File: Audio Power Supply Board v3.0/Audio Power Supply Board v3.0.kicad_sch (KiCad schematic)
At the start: 8 parts, among them J1 Conn_01x03_Female

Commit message: Change to a modular drawing and design
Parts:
- added C5, C6, C7, C8: 680µF/200V, Capacitor_THT:CP_Radial_D25.0mm_P10.00mm_SnapIn, symbol Device:C_Polarized_Small
- added D10, D11: 1N4001, Diode_THT:D_DO-41_SOD81_P10.16mm_Horizontal, symbol Diode:1N4001
- added D4, D5: D_x2_KCom_AKA_ALT, symbol Userlibrary:D_x2_KCom_AKA_ALT
- added D6, D7, D8, D9: MBR340, Diode_THT:D_DO-201AD_P15.24mm_Horizontal, symbol Diode:MBR340
- added J10, J11: Conn_01x10_Male, symbol Connector:Conn_01x11_Male
- added J12: Conn_01x12_Male, symbol Connector:Conn_01x12_Male
- added J2, J3: Conn_01x02_Male, symbol Connector:Conn_01x02_Male
- added J4, J5, J6, J7, J8, J9: Conn_01x01_Male, symbol Connector:Conn_01x01_Male
- added L1: Half_Bridge_Transformer, symbol Userlibrary:Half_Bridge_Transformer
- added R1, R2: 220k, symbol Device:R
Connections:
- net Power Switcher/V/2: now reaches C1.2, C2.1, C3.2, C4.1
- net A1 renamed Aux Supply/In1
- net A2 renamed Aux Supply/In2
- net Controller/Vb renamed +Vb
- net L renamed Netzfilter/L
- net L1 renamed Inrush Current Limiter/L1
- net N renamed Netzfilter/N
- net Sense renamed Inrush Current Limiter/Sense
- new net: J10.4 (Pin_4), J11.3 (Pin_3)
- new net: D10.2 (A), D11.2 (A), D6.2 (A), D8.1 (K), L1.18
- new net: C5.1, C7.1, D4.2, J4.1 (Pin_1), J5.1 (Pin_1), R1.1
- new net: C6.2, C8.2, J8.1 (Pin_1), J9.1 (Pin_1), L1.11, R2.2
- new net: D7.2 (A), D9.1 (K), L1.16
- new net: D5.3 (A), L1.10
- new net: D5.1 (A), L1.12
- new net: D4.3 (A), L1.13
- new net: D4.1 (A), L1.15
- new net ACLP: J10.6 (Pin_6)
- new net ADC: J10.7 (Pin_7)
- new net ASIG: J10.5 (Pin_5)
- new net BCLP: J11.6 (Pin_6)
- new net BDC: J11.7 (Pin_7)
- new net BSIG: J11.5 (Pin_5)
- new net Fan Control/FAN-: J2.2 (Pin_2), J3.2 (Pin_2)
- new net GND: J10.10 (Pin_10), J11.10 (Pin_10), J11.2 (Pin_2), J2.1 (Pin_1), J3.1 (Pin_1)
- new net GNDS: C5.2, C6.1, C7.2, C8.1, D5.2, J6.1 (Pin_1), J7.1 (Pin_1), L1.14, R1.2, R2.1
- new net MUTE: J10.8 (Pin_8), J11.8 (Pin_8)
- new net Mute Control/GND: L1.17
- new net Mute Control/V+1: D10.1 (K)
- new net Mute Control/V+2: D11.1 (K)
- new net PAH1: J10.3 (Pin_3)
- new net PAH2: J11.4 (Pin_4)
- new net PRE1: J10.1 (Pin_1)
- new net PRE2: J10.2 (Pin_2), J11.1 (Pin_1)
- new net Power Switcher/L1: L1.1, L1.2
- new net Power Switcher/L2: L1.3, L1.4
- new net Secondary Power/+15V: J10.9 (Pin_9), J11.9 (Pin_9)
- new net Secondary Power/+24V: J12.1 (Pin_1)
- new net Secondary Power/-15V: J10.11 (Pin_11), J11.11 (Pin_11)
- new net Secondary Power/V+: D6.1 (K), D7.1 (K)
- new net Secondary Power/V-: D8.2 (A), D9.2 (A)
- no-connect marks 0 -> 5
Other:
- removed sheet Main Power
- added sheet PrimaryProtection (Primaryprot.kicad_sch)
- sheet Controller ports: added Ho; removed HO
- sheet Fan Control ports: added -24V, FAN-, GND, PAH1, PAH2; removed none
- sheet Inrush Current Limiter ports: added L1, L2, Sense; removed none
- sheet Mute Control ports: added GND, MUTE, MUTEIN, V+1, V+2; removed none
- sheet Netzfilter ports: added A1, A2, L, N, PE; removed none
- sheet Power Switcher ports: added +Vb, CS+, CS-, GND, Ho, L1, L2, Lo, Vs, V/2; removed none
- sheet Secondary Power ports: added +15V, +24V, -15V, -24V, GND, V+, V-, VGND; removed none

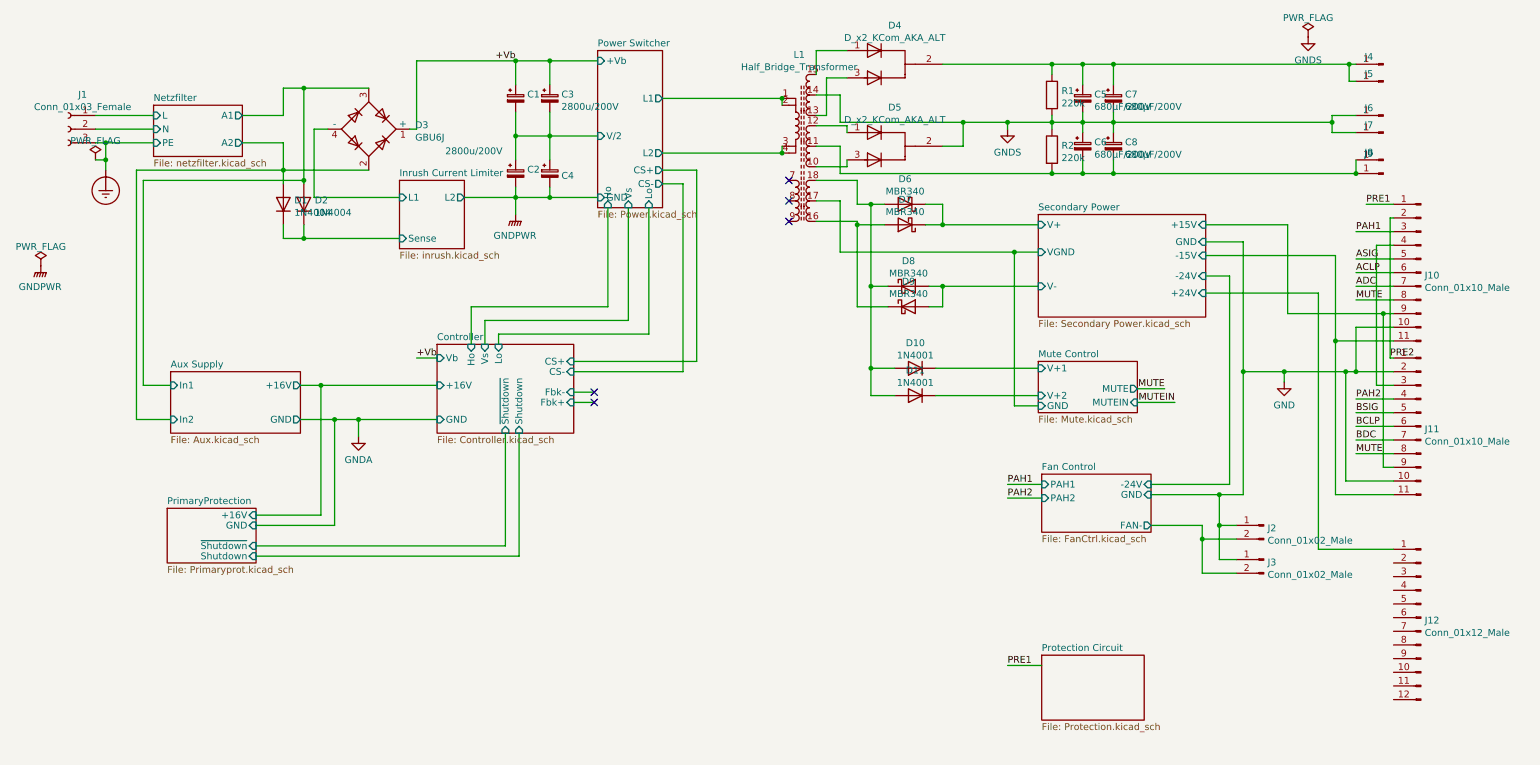
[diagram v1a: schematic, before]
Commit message: Add protection circuits
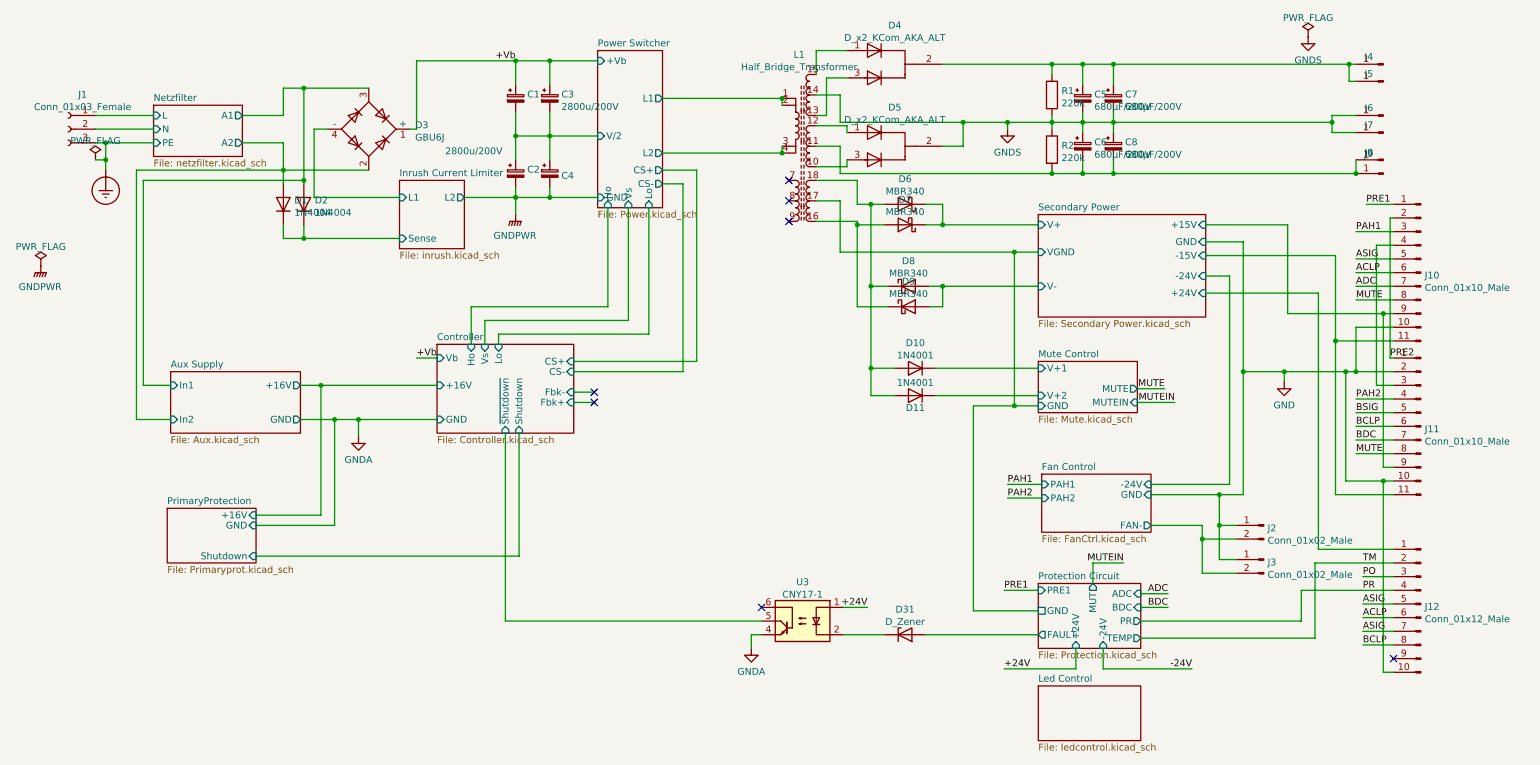
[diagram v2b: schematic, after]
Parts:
- added D31: D_Zener, symbol Device:D_Zener
- added U3: CNY17-1, symbol Isolator:CNY17-1
- J12: symbol Connector:Conn_01x12_Male -> Connector:Conn_01x10_Male
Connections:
- net ACLP: now also J12.6 (Pin_6)
- net ASIG: now also J12.5 (Pin_5), J12.7 (Pin_7)
- net BCLP: now also J12.8 (Pin_8)
- net Controller/~Shutdown: now also U3.5
- net GND: now also J12.10 (Pin_10)
- net GNDA: now also U3.4
- net TM: now reaches J12.2 (Pin_2)
- net PO: now reaches J12.3 (Pin_3)
- net PR: now reaches J12.4 (Pin_4)
- new net: D31.1 (K), U3.2
- new net +24V: U3.1
- new net Protection Circuit/FAULT: D31.2 (A)
- no-connect marks 5 -> 7
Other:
- added sheet Led Control (ledcontrol.kicad_sch)
- sheet PrimaryProtection ports: added none; removed ~Shutdown
- sheet Protection Circuit ports: added +24V, -24V, ADC, BDC, FAULT, GND, MUT, PR, PRE1, TEMP; removed none
